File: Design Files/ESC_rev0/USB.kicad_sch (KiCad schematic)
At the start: 9 parts, among them J8 USB_C_Receptacle_USB2.0_16P

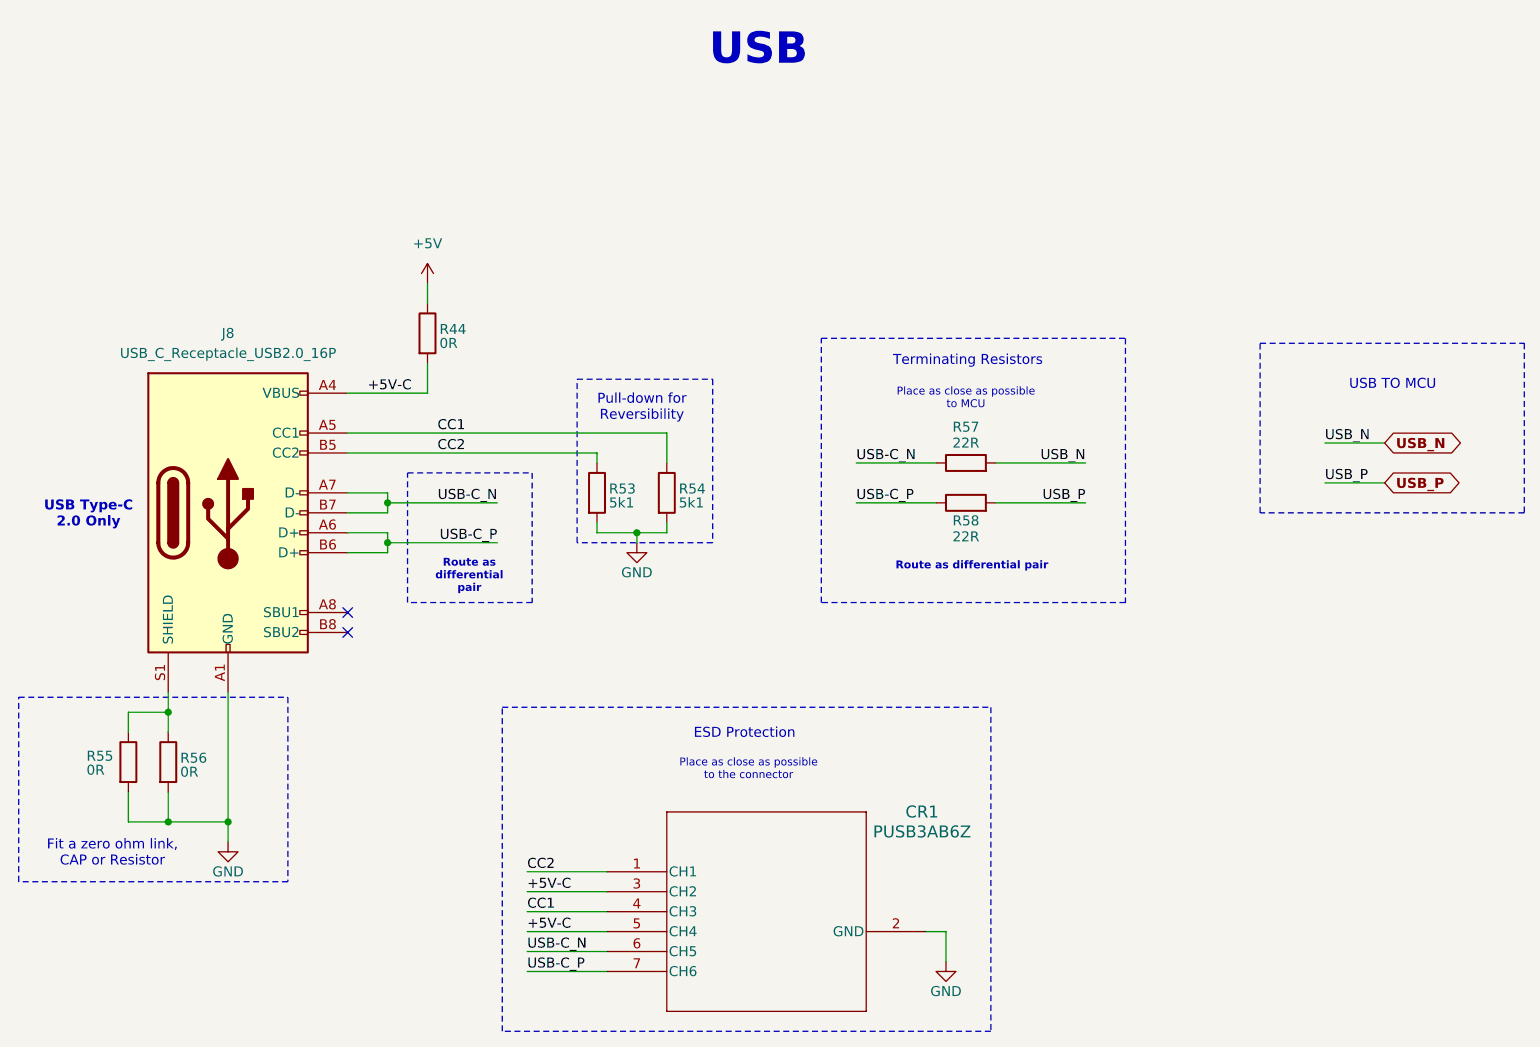
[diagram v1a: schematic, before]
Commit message: UPDATE 12
started schematics revision: edit and added info and circuits to some pages and assigned some footprints for components
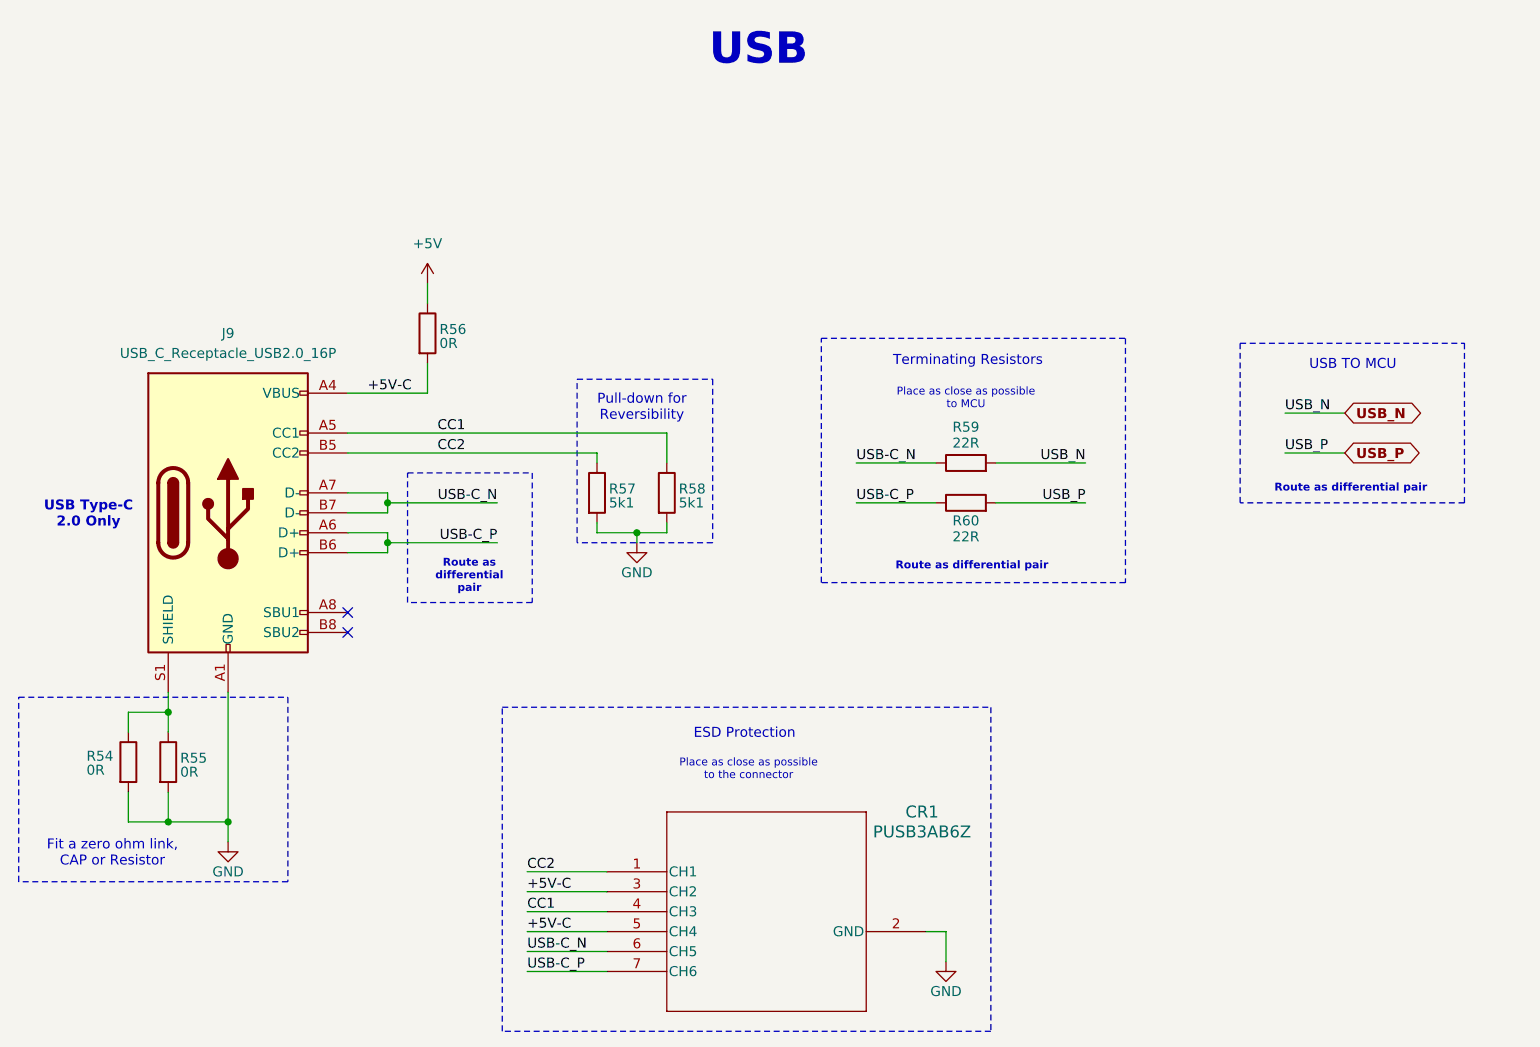
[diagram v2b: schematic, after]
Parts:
- CR1: footprint PUSB3AB6Z_NEX -> PUSB3AB6Z_foot:PUSB3AB6Z_NEX
- renumbered J8 to J9, R55 to R54, R56 to R55, R44 to R56, R53 to R57, R54 to R58, R57 to R59, R58 to R60

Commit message: update 13
assigned all footprints (provisionally) and imported them - errors and warning occurred, must be corrected in the future
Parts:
- J9: footprint (none) -> Connector_USB:USB_C_Receptacle_GCT_USB4105-xx-A_16P_TopMnt_Horizontal
- R54, R55, R56, R57, R58, R59, R60: footprint (none) -> Resistor_SMD:R_0603_1608Metric
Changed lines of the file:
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@@
 			)
 		)
-		(property "Footprint" ""
+		(property "Footprint" "Connector_USB:USB_C_Receptacle_GCT_USB4105-xx-A_16P_TopMnt_Horizontal"
 			(at 87.63 85.09 0)
 			(effects
@@
 			)
 		)
-		(property "Footprint" ""
+		(property "Footprint" "Resistor_SMD:R_0603_1608Metric"
 			(at 107.442 62.23 90)
 			(effects
@@
 			)
 		)
-		(property "Footprint" ""
+		(property "Footprint" "Resistor_SMD:R_0603_1608Metric"
 			(at 177.8 80.518 90)
 			(effects
@@
 			)
 		)
-		(property "Footprint" ""
+		(property "Footprint" "Resistor_SMD:R_0603_1608Metric"
 			(at 177.8 85.598 90)
 			(effects
@@
 			)
 		)
-		(property "Footprint" ""
+		(property "Footprint" "Resistor_SMD:R_0603_1608Metric"
 			(at 129.032 82.55 90)
 			(effects
@@
 			)
 		)
-		(property "Footprint" ""
+		(property "Footprint" "Resistor_SMD:R_0603_1608Metric"
 			(at 74.422 116.84 90)
 			(effects
@@
 			)
 		)
-		(property "Footprint" ""
+		(property "Footprint" "Resistor_SMD:R_0603_1608Metric"
 			(at 137.922 82.55 90)
 			(effects
@@
 			)
 		)
-		(property "Footprint" ""
+		(property "Footprint" "Resistor_SMD:R_0603_1608Metric"
 			(at 69.342 116.84 90)
 			(effects

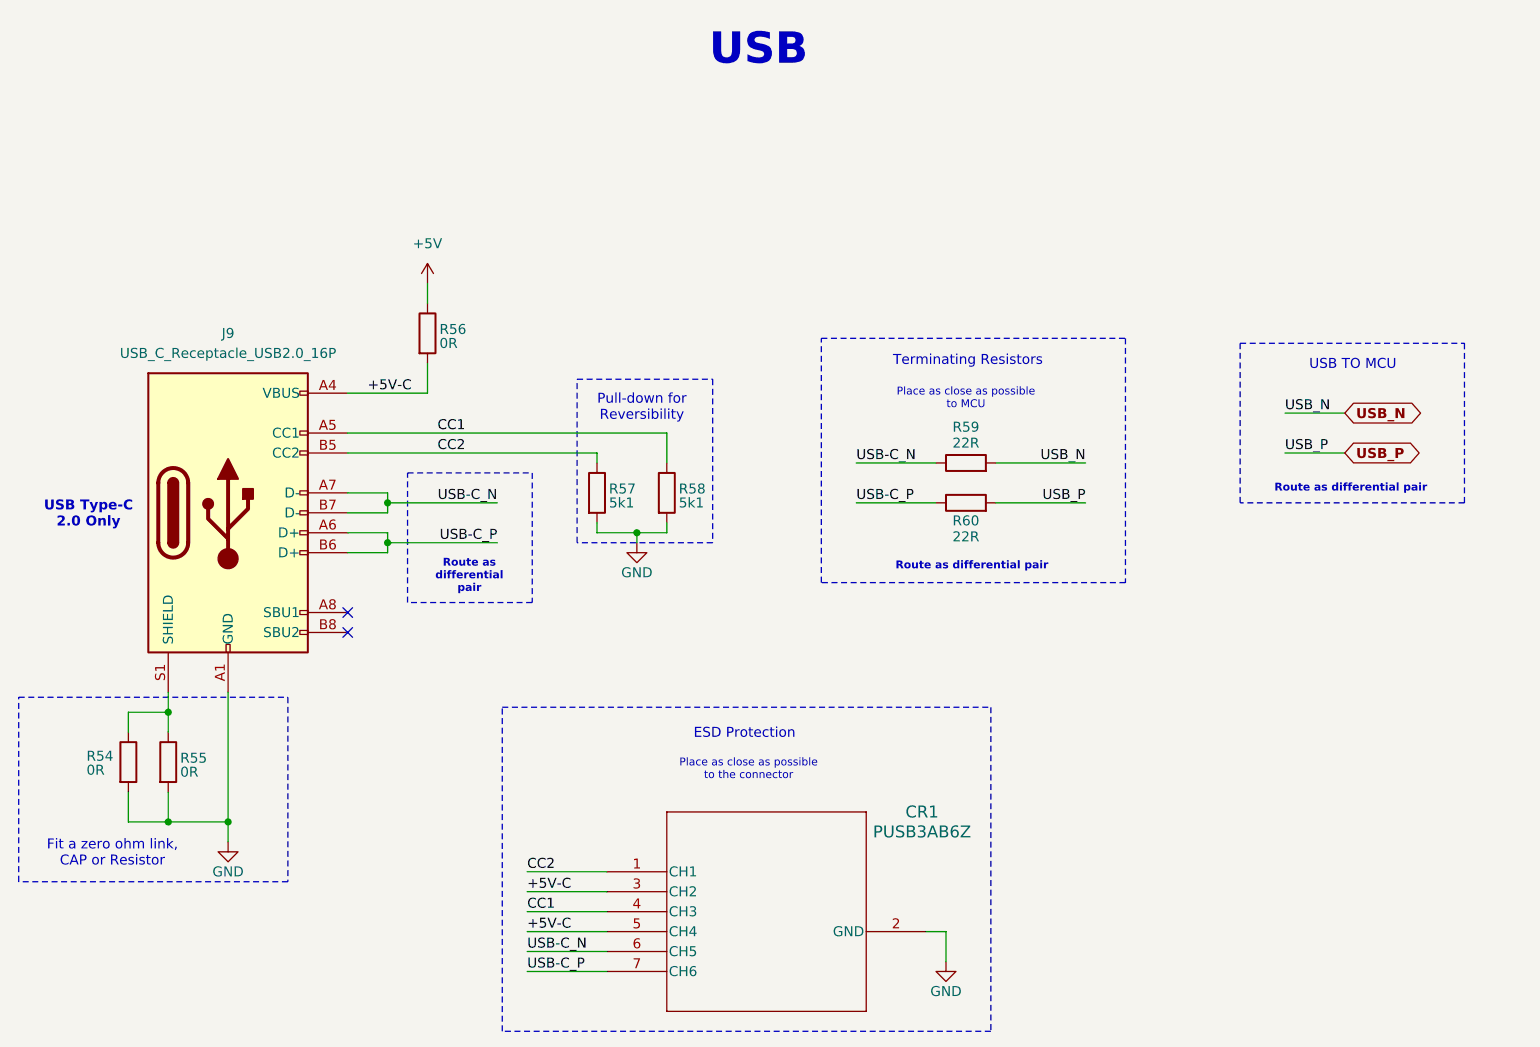
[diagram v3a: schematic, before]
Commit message: update 16
All components placed on board. Some components modifications and addition were made: added 3D models, changed some symbols and footprints positions and some component types.
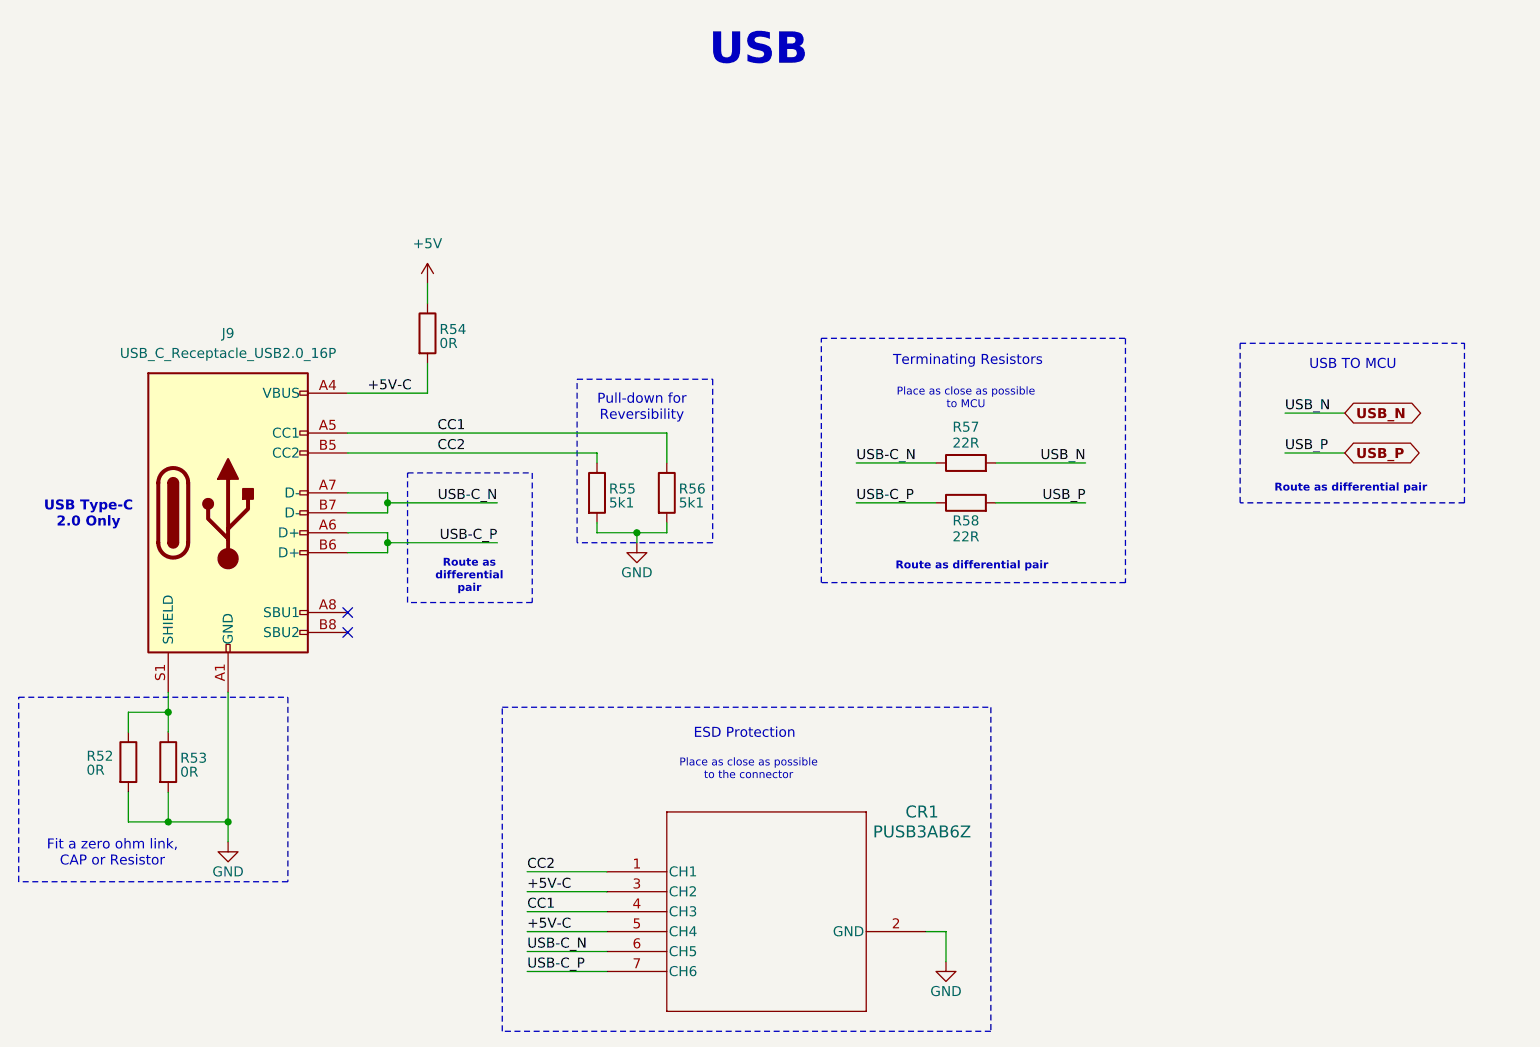
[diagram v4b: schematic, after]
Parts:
- renumbered R54 to R52, R55 to R53, R56 to R54, R57 to R55, R58 to R56, R59 to R57, R60 to R58
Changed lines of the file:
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@@
 		(on_board yes)
 		(dnp no)
-		(property "Reference" "#PWR082"
+		(property "Reference" "#PWR078"
 			(at 83.82 133.35 0)
 			(effects
@@
 			(project "ESC_rev0"
 				(path "/7906e740-34c4-4b06-b70f-1daa08872946/8b15351f-2572-408e-9e89-2ad0d13cef6d"
-					(reference "#PWR082")
+					(reference "#PWR078")
 					(unit 1)
 				)
@@
 		(on_board yes)
 		(dnp no)
-		(property "Reference" "R56"
+		(property "Reference" "R54"
 			(at 110.744 61.7221 0)
 			(effects
@@
 			(project ""
 				(path "/7906e740-34c4-4b06-b70f-1daa08872946/8b15351f-2572-408e-9e89-2ad0d13cef6d"
-					(reference "R56")
+					(reference "R54")
 					(unit 1)
 				)
@@
 		(on_board yes)
 		(dnp no)
-		(property "Reference" "R59"
+		(property "Reference" "R57"
 			(at 177.8 74.168 90)
 			(effects
@@
 			(project ""
 				(path "/7906e740-34c4-4b06-b70f-1daa08872946/8b15351f-2572-408e-9e89-2ad0d13cef6d"
-					(reference "R59")
+					(reference "R57")
 					(unit 1)
 				)
@@
 		(on_board yes)
 		(dnp no)
-		(property "Reference" "R60"
+		(property "Reference" "R58"
 			(at 177.8 86.106 90)
 			(effects
@@
 			(project "ESC_rev0"
 				(path "/7906e740-34c4-4b06-b70f-1daa08872946/8b15351f-2572-408e-9e89-2ad0d13cef6d"
-					(reference "R60")
+					(reference "R58")
 					(unit 1)
 				)
@@
 		(on_board yes)
 		(dnp no)
-		(property "Reference" "#PWR085"
+		(property "Reference" "#PWR081"
 			(at 175.26 148.59 0)
 			(effects
@@
 			(project "ESC_rev0"
 				(path "/7906e740-34c4-4b06-b70f-1daa08872946/8b15351f-2572-408e-9e89-2ad0d13cef6d"
-					(reference "#PWR085")
+					(reference "#PWR081")
 					(unit 1)
 				)
@@
 		(dnp no)
 		(fields_autoplaced yes)
-		(property "Reference" "#PWR083"
+		(property "Reference" "#PWR079"
 			(at 109.22 59.69 0)
 			(effects
@@
 			(project ""
 				(path "/7906e740-34c4-4b06-b70f-1daa08872946/8b15351f-2572-408e-9e89-2ad0d13cef6d"
-					(reference "#PWR083")
+					(reference "#PWR079")
 					(unit 1)
 				)
@@
 		(on_board yes)
 		(dnp no)
-		(property "Reference" "R57"
+		(property "Reference" "R55"
 			(at 132.334 82.0421 0)
 			(effects
@@
 			(project "ESC_rev0"
 				(path "/7906e740-34c4-4b06-b70f-1daa08872946/8b15351f-2572-408e-9e89-2ad0d13cef6d"
-					(reference "R57")
+					(reference "R55")
 					(unit 1)
 				)
@@
 		(on_board yes)
 		(dnp no)
-		(property "Reference" "#PWR084"
+		(property "Reference" "#PWR080"
 			(at 135.89 95.25 0)
 			(effects
@@
 			(project ""
 				(path "/7906e740-34c4-4b06-b70f-1daa08872946/8b15351f-2572-408e-9e89-2ad0d13cef6d"
-					(reference "#PWR084")
+					(reference "#PWR080")
 					(unit 1)
 				)
@@
 		(on_board yes)
 		(dnp no)
-		(property "Reference" "R55"
+		(property "Reference" "R53"
 			(at 77.724 116.3321 0)
 			(effects
@@
 			(project "ESC_rev0"
 				(path "/7906e740-34c4-4b06-b70f-1daa08872946/8b15351f-2572-408e-9e89-2ad0d13cef6d"
-					(reference "R55")
+					(reference "R53")
 					(unit 1)
 				)
@@
 		(on_board yes)
 		(dnp no)
-		(property "Reference" "R58"
+		(property "Reference" "R56"
 			(at 141.224 82.0421 0)
 			(effects
@@
 			(project "ESC_rev0"
 				(path "/7906e740-34c4-4b06-b70f-1daa08872946/8b15351f-2572-408e-9e89-2ad0d13cef6d"
-					(reference "R58")
+					(reference "R56")
 					(unit 1)
 				)
@@
 		(on_board yes)
 		(dnp no)
-		(property "Reference" "R54"
+		(property "Reference" "R52"
 			(at 65.786 116.0781 0)
 			(effects
@@
 			(project "ESC_rev0"
 				(path "/7906e740-34c4-4b06-b70f-1daa08872946/8b15351f-2572-408e-9e89-2ad0d13cef6d"
-					(reference "R54")
-					(unit 1)
-				)
+					(reference "R52")
+					(unit 1)
+				)

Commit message: update 21
DRC checked, all problems solved. Created Custom Rules to following JLCPCB most important capabilities. Relevant modifications on tracks, components positions and to copper pours were made. Board images were updated in the schematics.
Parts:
- J9: footprint Connector_USB:USB_C_Receptacle_GCT_USB4105-xx-A_16P_TopMnt_Horizontal -> Connector_USB:USB_C_Receptacle_GCT_USB4105-xx-A_16P_TopMnt_Horizontal_mod
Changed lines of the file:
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@@
 	(title_block
 		(title "USB")
+		(date "2025-01-24")
 		(rev "0")
 	)
@@
 			)
 		)
-		(property "Footprint" "Connector_USB:USB_C_Receptacle_GCT_USB4105-xx-A_16P_TopMnt_Horizontal"
+		(property "Footprint" "Connector_USB:USB_C_Receptacle_GCT_USB4105-xx-A_16P_TopMnt_Horizontal_mod"
 			(at 87.63 85.09 0)
 			(effects
